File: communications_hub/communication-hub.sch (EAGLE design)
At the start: 43 parts, among them CON1 SM04B-GHS-TB, CON2 SM04B-GHS-TB, CON3 SM02B-GHS-TB, CON4 SM03B-GHS-TB, CON5 SM03B-GHS-TB, U1 TCAN1042HVDR, U2 TCAN1042HVDR

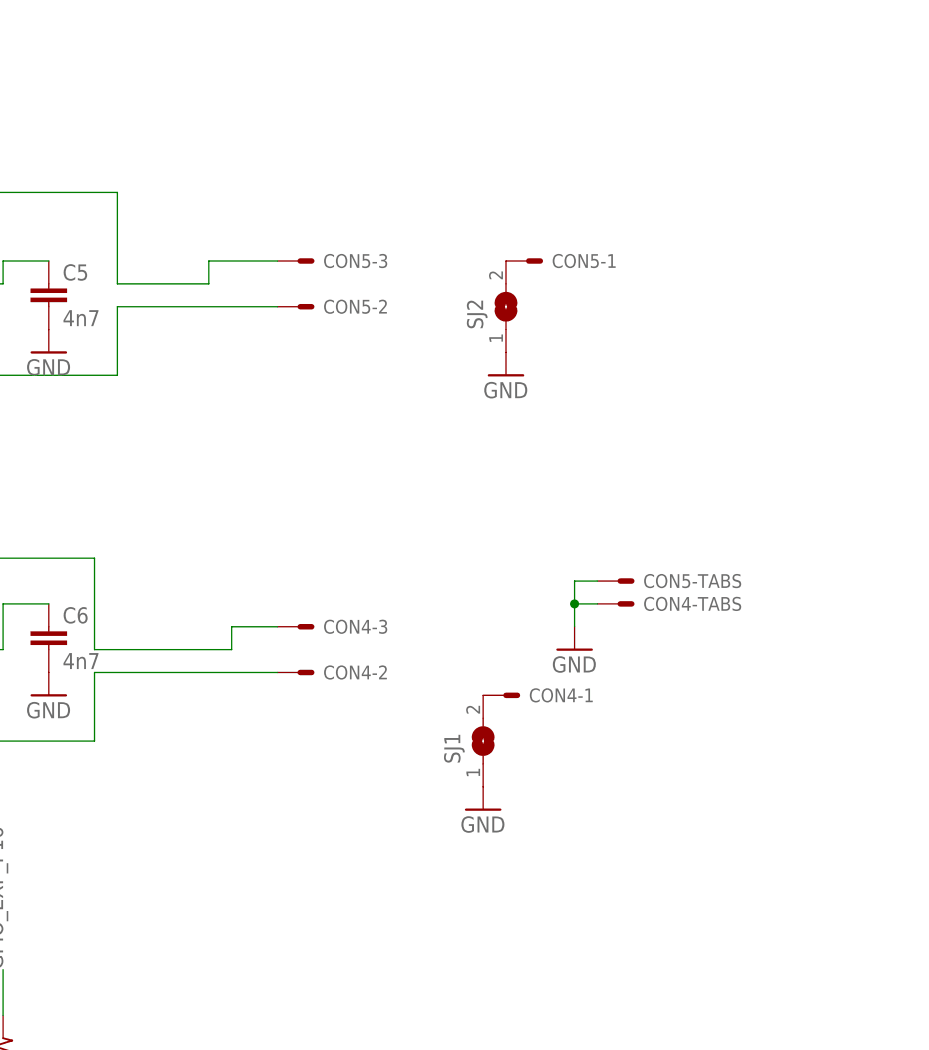
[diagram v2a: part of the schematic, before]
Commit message: Added 5V pin to CAN connectors in case ESC CAN transceivers require external 5V
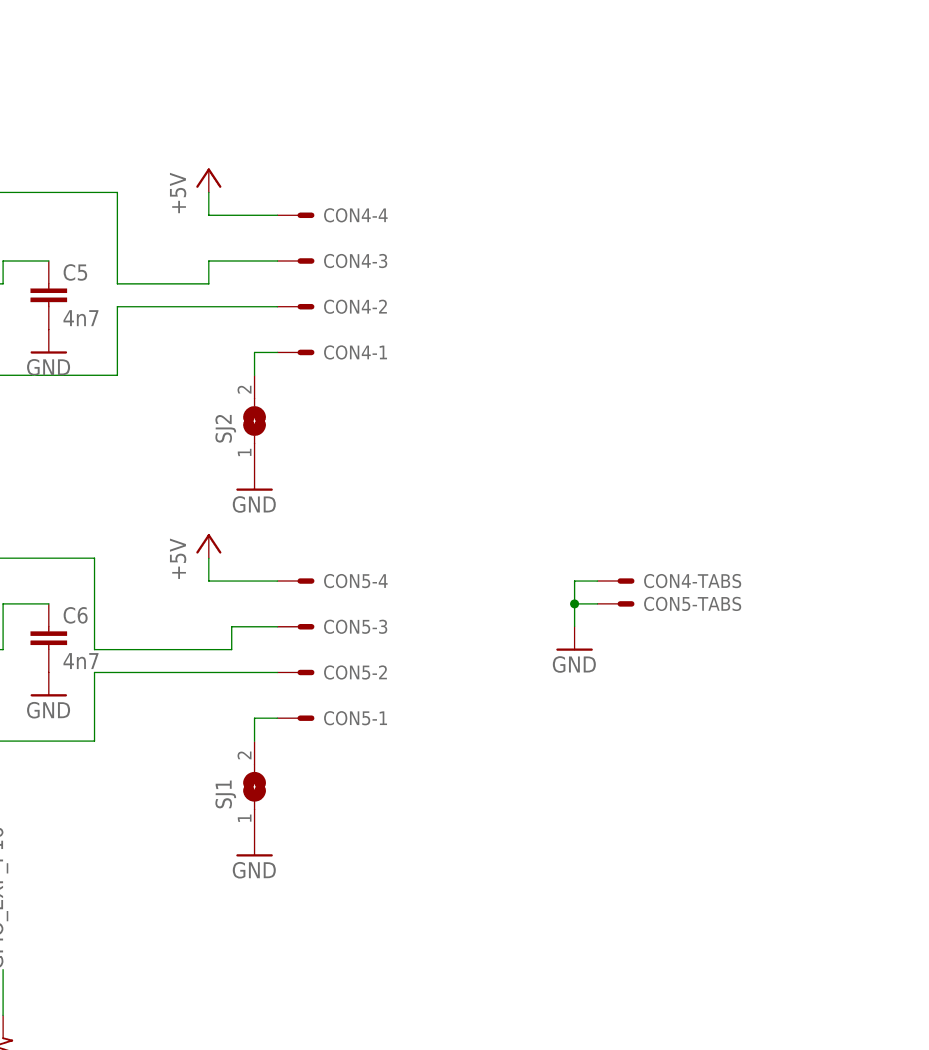
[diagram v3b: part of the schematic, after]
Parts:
- CON4, CON5: value SM03B-GHS-TB -> SM04B-GHS-TB; device ARVP:SM03B-GHS-TB -> ARVP:SM04B-GHS-TB
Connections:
- removed net N$31: CON5-1.S, SJ2.2
- removed net N$32: CON4-1.S, SJ1.2
- new net N$7: CON5-1.S, SJ1.2
- new net N$8: CON4-1.S, SJ2.2
- net +5V: now also CON4-4.S, CON5-4.S
- net N$21: now also CON5-3.S; no longer CON4-3.S
- net N$22: now also CON5-2.S; no longer CON4-2.S
- net N$23: now also CON4-3.S; no longer CON5-3.S
- net N$24: now also CON4-2.S; no longer CON5-2.S
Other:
- moved on the sheet: CON4-1, CON4-2, CON4-3, CON4-TABS, CON5-1, CON5-2, CON5-3, CON5-TABS, SJ1, SJ2
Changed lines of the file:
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@@
 <part name="R16" library="resistor" library_urn="urn:adsk.eagle:library:348" deviceset="R-EU_" device="R1206" package3d_urn="urn:adsk.eagle:package:26062/1" value="60"/>
 <part name="R17" library="resistor" library_urn="urn:adsk.eagle:library:348" deviceset="R-EU_" device="R1206" package3d_urn="urn:adsk.eagle:package:26062/1" value="60"/>
-<part name="CON5" library="ARVP" deviceset="SM03B-GHS-TB" device=""/>
-<part name="CON4" library="ARVP" deviceset="SM03B-GHS-TB" device=""/>
 <part name="SJ2" library="jumper" library_urn="urn:adsk.eagle:library:252" deviceset="SJ" device="" package3d_urn="urn:adsk.eagle:package:15471/1"/>
 <part name="SJ1" library="jumper" library_urn="urn:adsk.eagle:library:252" deviceset="SJ" device="" package3d_urn="urn:adsk.eagle:package:15471/1"/>
@@
 <part name="GND28" library="supply1" library_urn="urn:adsk.eagle:library:371" deviceset="GND" device=""/>
 <part name="FRAME1" library="frames" library_urn="urn:adsk.eagle:library:229" deviceset="TABL_L" device=""/>
+<part name="CON4" library="ARVP" deviceset="SM04B-GHS-TB" device=""/>
+<part name="CON5" library="ARVP" deviceset="SM04B-GHS-TB" device=""/>
+<part name="P+5" library="supply1" library_urn="urn:adsk.eagle:library:371" deviceset="+5V" device=""/>
+<part name="P+6" library="supply1" library_urn="urn:adsk.eagle:library:371" deviceset="+5V" device=""/>
 </parts>
 <sheets>
@@
 <instance part="R16" gate="G$1" x="238.76" y="162.56" rot="R90"/>
 <instance part="R17" gate="G$1" x="238.76" y="152.4" rot="R90"/>
-<instance part="CON5" gate="-1" x="299.72" y="200.66"/>
-<instance part="CON5" gate="-2" x="274.32" y="195.58"/>
-<instance part="CON5" gate="-3" x="274.32" y="200.66"/>
-<instance part="CON5" gate="-TABS" x="309.88" y="165.1"/>
-<instance part="CON4" gate="-1" x="297.18" y="152.4"/>
-<instance part="CON4" gate="-2" x="274.32" y="154.94"/>
-<instance part="CON4" gate="-3" x="274.32" y="160.02"/>
-<instance part="CON4" gate="-TABS" x="309.88" y="162.56"/>
-<instance part="SJ2" gate="1" x="299.72" y="195.58" rot="R90"/>
-<instance part="SJ1" gate="1" x="297.18" y="147.32" rot="R90"/>
-<instance part="GND26" gate="1" x="297.18" y="139.7"/>
-<instance part="GND27" gate="1" x="299.72" y="187.96"/>
+<instance part="SJ2" gate="1" x="271.78" y="182.88" rot="R90"/>
+<instance part="SJ1" gate="1" x="271.78" y="142.24" rot="R90"/>
+<instance part="GND26" gate="1" x="271.78" y="134.62"/>
+<instance part="GND27" gate="1" x="271.78" y="175.26"/>
 <instance part="JP4" gate="A" x="152.4" y="142.24" rot="R90"/>
 <instance part="JP3" gate="A" x="152.4" y="182.88" rot="R90"/>
@@
 <instance part="FRAME1" gate="G$1" x="0" y="0"/>
 <instance part="FRAME1" gate="G$2" x="299.72" y="0"/>
+<instance part="CON4" gate="-1" x="274.32" y="190.5" rot="MR180"/>
+<instance part="CON4" gate="-2" x="274.32" y="195.58" rot="MR180"/>
+<instance part="CON4" gate="-3" x="274.32" y="200.66" rot="MR180"/>
+<instance part="CON4" gate="-TABS" x="309.88" y="165.1"/>
+<instance part="CON4" gate="-4" x="274.32" y="205.74" rot="MR180"/>
+<instance part="CON5" gate="-1" x="274.32" y="149.86" rot="MR180"/>
+<instance part="CON5" gate="-2" x="274.32" y="154.94" rot="MR180"/>
+<instance part="CON5" gate="-3" x="274.32" y="160.02" rot="MR180"/>
+<instance part="CON5" gate="-TABS" x="309.88" y="162.56"/>
+<instance part="CON5" gate="-4" x="274.32" y="165.1" rot="MR180"/>
+<instance part="P+5" gate="1" x="266.7" y="210.82"/>
+<instance part="P+6" gate="1" x="266.7" y="170.18"/>
 </instances>
 <busses>
@@
 <pinref part="GND28" gate="1" pin="GND"/>
 <wire x1="307.34" y1="160.02" x2="307.34" y2="162.56" width="0.1524" layer="91"/>
-<pinref part="CON4" gate="-TABS" pin="S"/>
 <wire x1="307.34" y1="162.56" x2="309.88" y2="162.56" width="0.1524" layer="91"/>
 <wire x1="307.34" y1="162.56" x2="307.34" y2="165.1" width="0.1524" layer="91"/>
-<pinref part="CON5" gate="-TABS" pin="S"/>
 <wire x1="307.34" y1="165.1" x2="309.88" y2="165.1" width="0.1524" layer="91"/>
 <junction x="307.34" y="162.56"/>
+<pinref part="CON4" gate="-TABS" pin="S"/>
+<pinref part="CON5" gate="-TABS" pin="S"/>
 </segment>
 </net>
@@
 <pinref part="JP26" gate="A" pin="8"/>
 <wire x1="119.38" y1="139.7" x2="109.22" y2="139.7" width="0.1524" layer="91"/>
+</segment>
+<segment>
+<wire x1="266.7" y1="205.74" x2="266.7" y2="208.28" width="0.1524" layer="91"/>
+<pinref part="P+5" gate="1" pin="+5V"/>
+<pinref part="CON4" gate="-4" pin="S"/>
+<wire x1="266.7" y1="205.74" x2="274.32" y2="205.74" width="0.1524" layer="91"/>
+</segment>
+<segment>
+<wire x1="266.7" y1="165.1" x2="266.7" y2="167.64" width="0.1524" layer="91"/>
+<pinref part="P+6" gate="1" pin="+5V"/>
+<pinref part="CON5" gate="-4" pin="S"/>
+<wire x1="266.7" y1="165.1" x2="274.32" y2="165.1" width="0.1524" layer="91"/>
 </segment>
 </net>
@@
 <junction x="238.76" y="167.64"/>
 <wire x1="269.24" y1="157.48" x2="269.24" y2="160.02" width="0.1524" layer="91"/>
-<pinref part="CON4" gate="-3" pin="S"/>
+<pinref part="CON5" gate="-3" pin="S"/>
 <wire x1="269.24" y1="160.02" x2="274.32" y2="160.02" width="0.1524" layer="91"/>
 </segment>
@@
 <pinref part="R17" gate="G$1" pin="1"/>
 <junction x="238.76" y="147.32"/>
-<pinref part="CON4" gate="-2" pin="S"/>
+<pinref part="CON5" gate="-2" pin="S"/>
 <wire x1="254" y1="154.94" x2="274.32" y2="154.94" width="0.1524" layer="91"/>
 </segment>
@@
 <pinref part="R14" gate="G$1" pin="2"/>
 <junction x="238.76" y="208.28"/>
-<pinref part="CON5" gate="-3" pin="S"/>
+<pinref part="CON4" gate="-3" pin="S"/>
 <wire x1="266.7" y1="200.66" x2="274.32" y2="200.66" width="0.1524" layer="91"/>
 </segment>
@@
 <pinref part="R15" gate="G$1" pin="1"/>
 <junction x="238.76" y="187.96"/>
-<pinref part="CON5" gate="-2" pin="S"/>
+<pinref part="CON4" gate="-2" pin="S"/>
 <wire x1="256.54" y1="195.58" x2="274.32" y2="195.58" width="0.1524" layer="91"/>
 </segment>
@@
 </segment>
 </net>
-<net name="N$31" class="0">
-<segment>
-<pinref part="CON5" gate="-1" pin="S"/>
-<pinref part="SJ2" gate="1" pin="2"/>
-</segment>
-</net>
-<net name="N$32" class="0">
-<segment>
-<pinref part="CON4" gate="-1" pin="S"/>
-<pinref part="SJ1" gate="1" pin="2"/>
-</segment>
-</net>
 <net name="N$33" class="0">
 <segment>
@@
 </segment>
 </net>
+<net name="N$7" class="0">
+<segment>
+<pinref part="SJ1" gate="1" pin="2"/>
+<wire x1="271.78" y1="149.86" x2="271.78" y2="147.32" width="0.1524" layer="91"/>
+<pinref part="CON5" gate="-1" pin="S"/>
+<wire x1="271.78" y1="149.86" x2="274.32" y2="149.86" width="0.1524" layer="91"/>
+</segment>
+</net>
+<net name="N$8" class="0">
+<segment>
+<pinref part="SJ2" gate="1" pin="2"/>
+<wire x1="271.78" y1="190.5" x2="271.78" y2="187.96" width="0.1524" layer="91"/>
+<pinref part="CON4" gate="-1" pin="S"/>
+<wire x1="271.78" y1="190.5" x2="274.32" y2="190.5" width="0.1524" layer="91"/>
+</segment>
+</net>

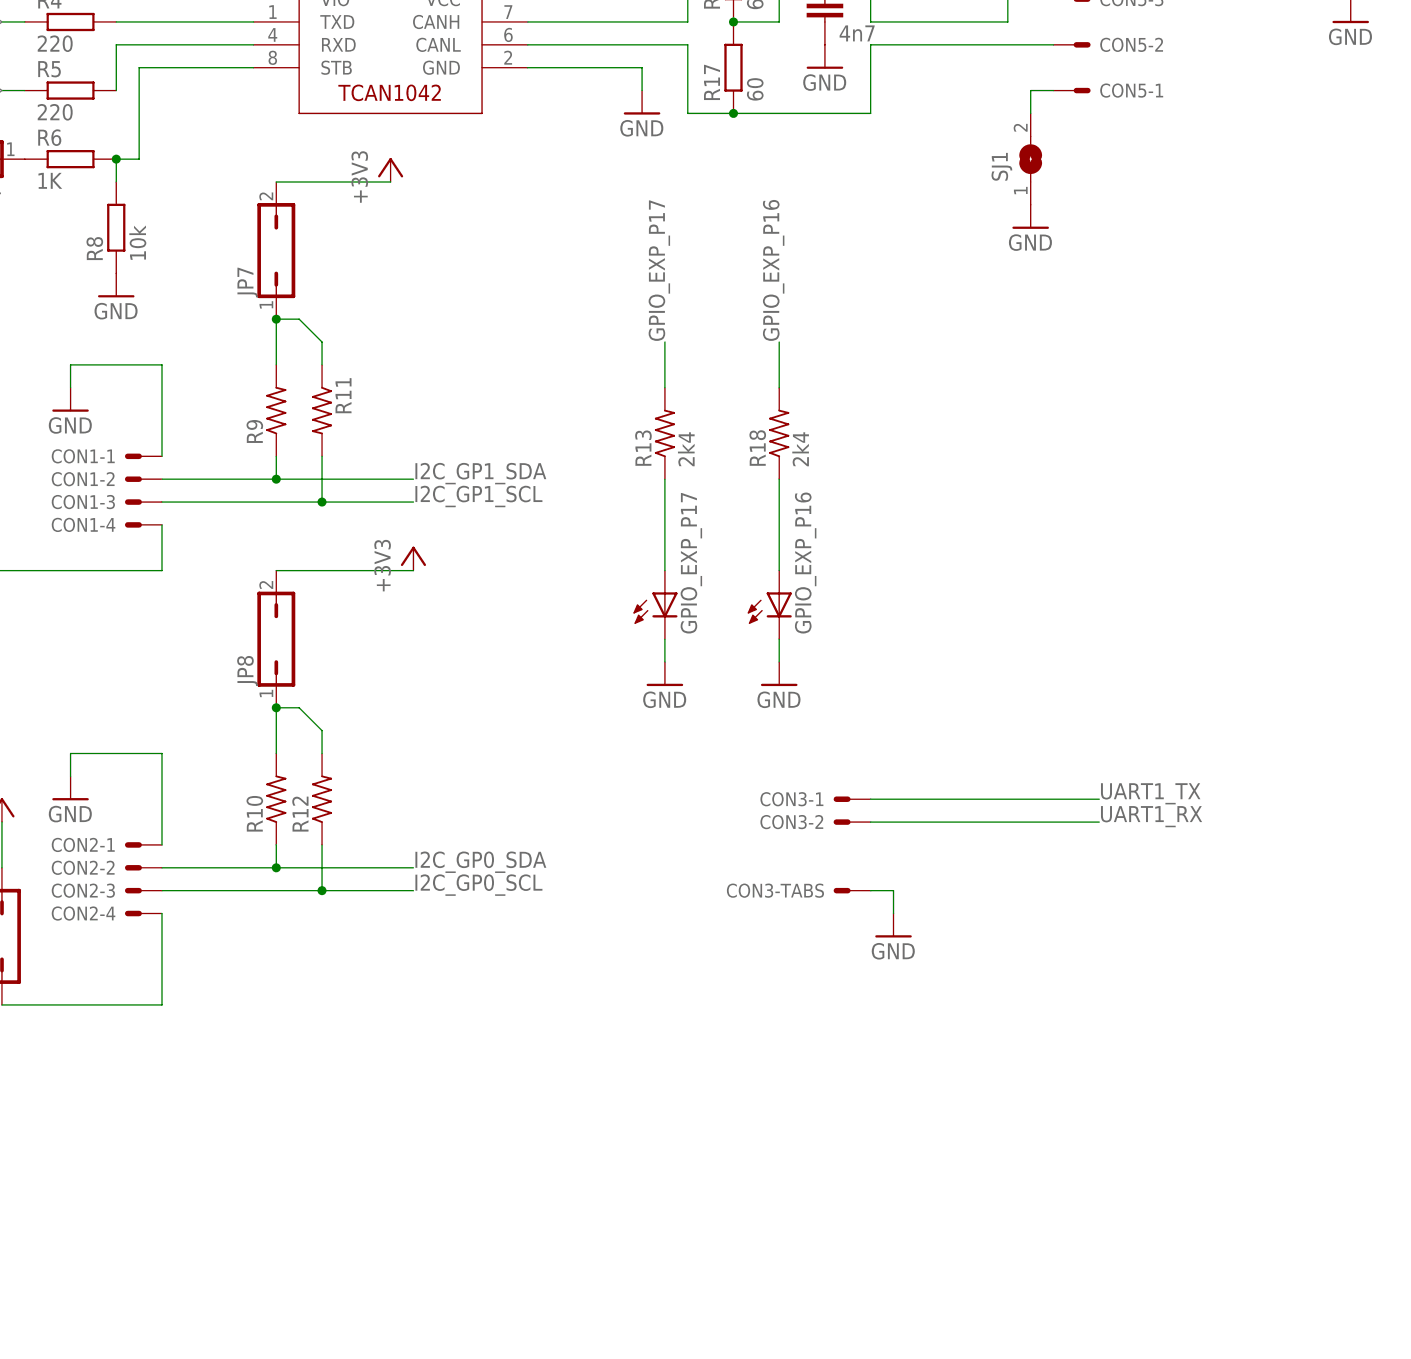
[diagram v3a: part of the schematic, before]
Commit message: Added new LEDs with transistor drivers for high brightness
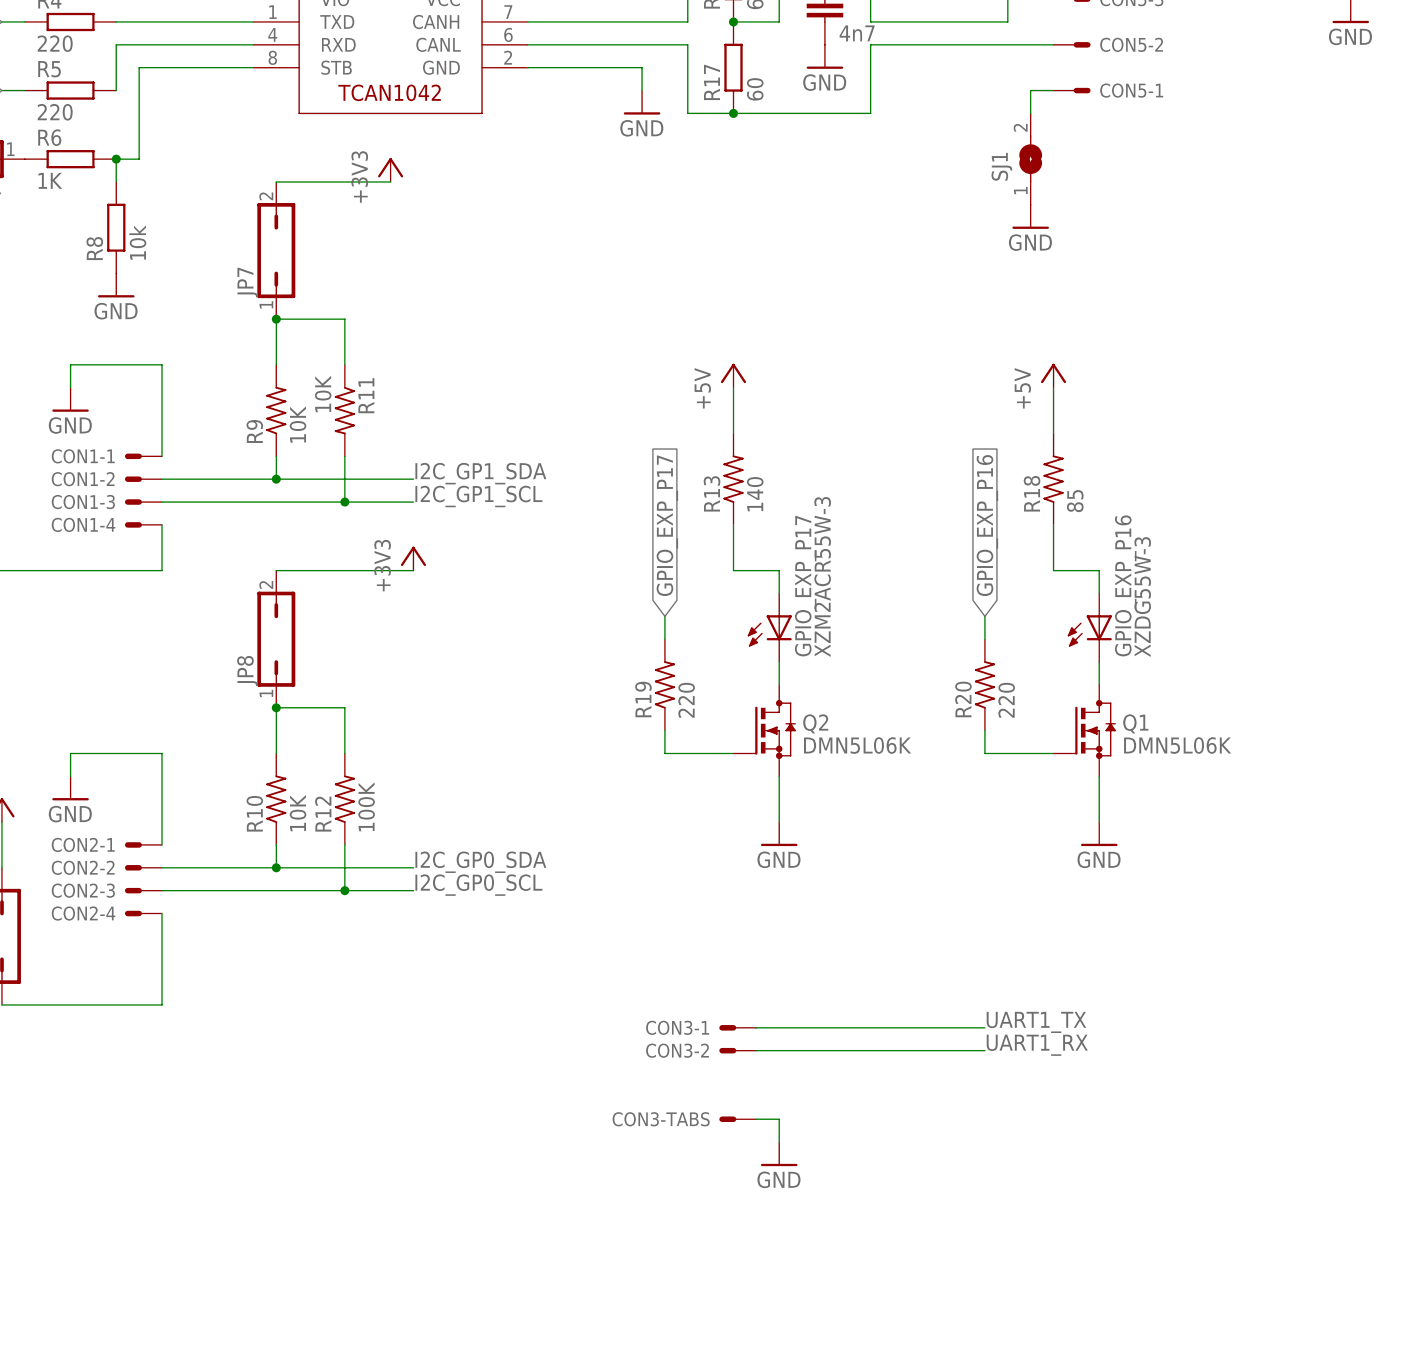
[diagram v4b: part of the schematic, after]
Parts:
- added Q1, Q2: DMN5L06K, transistor-small-signal:BSS123
- added R19, R20: 220, rcl:R-US_R0805
- GPIO_EXP_P16: value (none) -> XZDG55W-3
- GPIO_EXP_P17: value (none) -> XZM2ACR55W-3
- R10, R11, R9: value (none) -> 10K
- R12: value (none) -> 100K
- R13: value 2k4 -> 140
- R18: value 2k4 -> 85
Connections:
- new net N$10: GPIO_EXP_P16.C, Q1.D
- new net N$11: Q2.G, R19.1
- new net N$12: Q1.G, R20.1
- new net N$9: GPIO_EXP_P17.C, Q2.D
- net +5V: now also R13.2, R18.2
- net GND: now also Q1.S, Q2.S; no longer GPIO_EXP_P16.C, GPIO_EXP_P17.C
- net GPIO_EXP_P16: now also R20.2; no longer R18.2
- net GPIO_EXP_P17: now also R19.2; no longer R13.2
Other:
- moved on the sheet: CON3-1, CON3-2, CON3-TABS, GPIO_EXP_P16, GPIO_EXP_P17, R11, R12, R13, R18
